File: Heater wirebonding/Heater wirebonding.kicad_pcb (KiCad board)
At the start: 2 copper layers, 22.8 x 19.5 mm, 2 parts, among them J1 Conn_01x20_Pin, J2 TF31-20S-0.5SH_800_

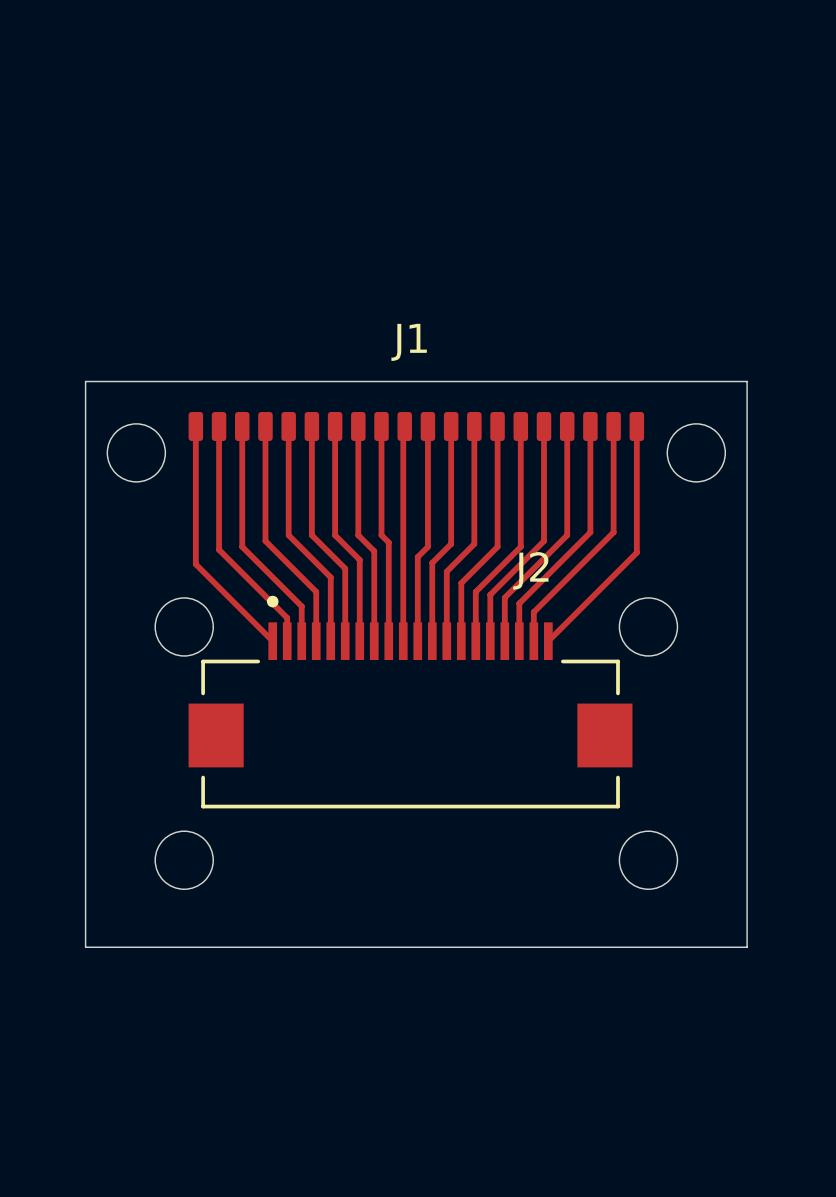
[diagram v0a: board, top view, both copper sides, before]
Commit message: Modified PCB layout to account for screw head
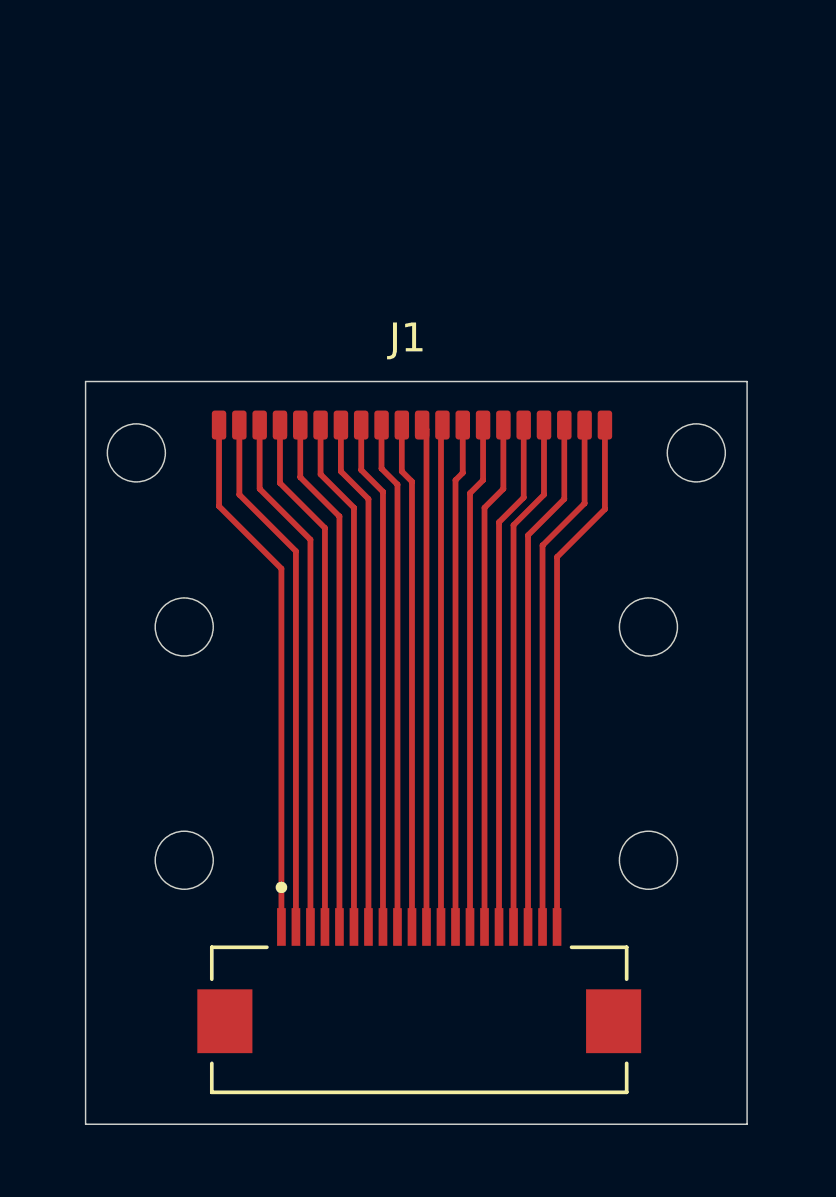
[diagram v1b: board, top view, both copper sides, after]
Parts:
- moved J2 9.85 mm to (160.0, 57.5)
- moved J1 0.16 mm to (159.6, 37.0)
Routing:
- net Net-(J1-Pin_9): track 7.50 -> 17.3 mm
- net Net-(J1-Pin_10): track 7.42 -> 17.2 mm
- net Net-(J1-Pin_8): track 7.63 -> 17.4 mm
- net Net-(J1-Pin_7): track 7.75 -> 17.5 mm
- net Net-(J1-Pin_6): track 7.88 -> 17.6 mm
- net Net-(J1-Pin_5): track 8.00 -> 17.7 mm
- net Net-(J1-Pin_4): track 8.12 -> 17.7 mm
- net Net-(J1-Pin_11): track 7.54 -> 17.2 mm
- net Net-(J1-Pin_3): track 8.25 -> 17.8 mm
- net Net-(J1-Pin_2): track 8.37 -> 17.9 mm
- net Net-(J1-Pin_1): track 8.50 -> 18.0 mm
- net Net-(J1-Pin_12): track 7.67 -> 17.1 mm
- net Net-(J1-Pin_13): track 7.79 -> 17.2 mm
- net Net-(J1-Pin_14): track 7.92 -> 17.3 mm
- net Net-(J1-Pin_15): track 8.04 -> 17.4 mm
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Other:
- board size 22.8 x 19.5 mm -> 22.8 x 25.6 mm

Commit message: Modified PCB design
Changed 4 wirebond pads to ground and filled in PCB GND zone. Changed PCB shape such that the PCB acts as the clamp for the chip.
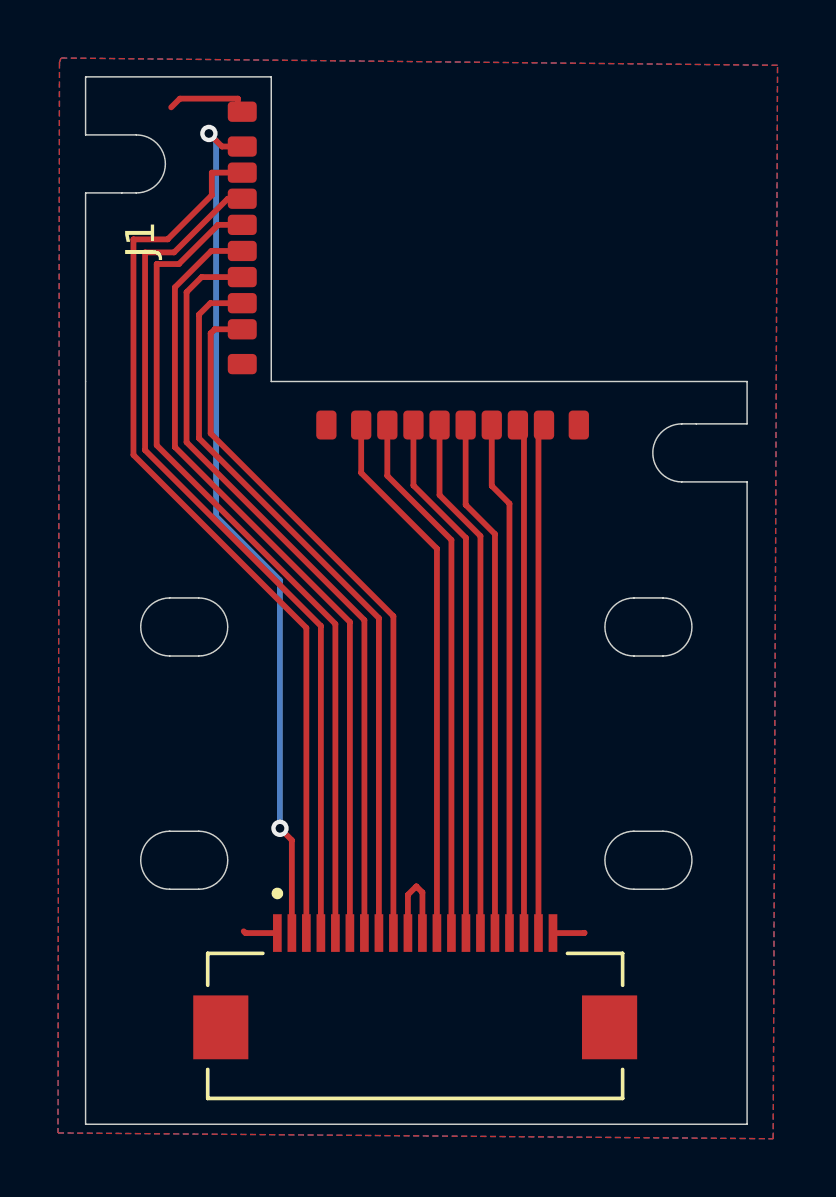
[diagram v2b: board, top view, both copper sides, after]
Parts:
- added J3: Conn_01x10_Pin, Custom_pads:Pads 1x10, F.Cu at (161.2, 37.0)
- J1: value Conn_01x20_Pin -> Conn_01x10_Pin; footprint Custom_pads:Pads 1x20 -> Custom_pads:Pads 1x10
- moved J1 8.57 mm to (153.9, 30.6), turned to 90 degrees
- moved J2 0.25 mm to (159.9, 57.7)
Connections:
- J1 pad 1: Net-(J1-Pin_1) -> GND
- J1 pad 10: Net-(J1-Pin_10) -> GND
- J2 pad 1: Net-(J1-Pin_1) -> GND
- J2 pad 10: Net-(J1-Pin_10) -> GND
- J2 pad 11: Net-(J1-Pin_11) -> GND
- J2 pad 12: Net-(J1-Pin_12) -> Net-(J3-Pin_9)
- J2 pad 13: Net-(J1-Pin_13) -> Net-(J3-Pin_8)
- J2 pad 14: Net-(J1-Pin_14) -> Net-(J3-Pin_7)
- J2 pad 15: Net-(J1-Pin_15) -> Net-(J3-Pin_6)
- J2 pad 16: Net-(J1-Pin_16) -> Net-(J3-Pin_5)
- J2 pad 17: Net-(J1-Pin_17) -> Net-(J3-Pin_4)
- J2 pad 18: Net-(J1-Pin_18) -> Net-(J3-Pin_3)
- J2 pad 19: Net-(J1-Pin_19) -> Net-(J3-Pin_2)
- J2 pad 2: Net-(J1-Pin_2) -> Net-(J1-Pin_9)
- J2 pad 20: Net-(J1-Pin_20) -> GND
- J2 pad 3: Net-(J1-Pin_3) -> Net-(J1-Pin_8)
- J2 pad 4: Net-(J1-Pin_4) -> Net-(J1-Pin_7)
- J2 pad 5: Net-(J1-Pin_5) -> Net-(J1-Pin_6)
- J2 pad 6: Net-(J1-Pin_6) -> Net-(J1-Pin_5)
- J2 pad 7: Net-(J1-Pin_7) -> Net-(J1-Pin_4)
- J2 pad 8: Net-(J1-Pin_8) -> Net-(J1-Pin_3)
- J2 pad 9: Net-(J1-Pin_9) -> Net-(J1-Pin_2)
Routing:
- net Net-(J3-Pin_9): track 0.00 -> 18.6 mm
- net Net-(J3-Pin_8): track 0.00 -> 18.4 mm
- net Net-(J3-Pin_7): track 0.00 -> 18.3 mm
- net Net-(J3-Pin_6): track 0.00 -> 18.1 mm
- net Net-(J1-Pin_1): track 18.0 -> 0.00 mm
- net Net-(J3-Pin_5): track 0.00 -> 17.9 mm
- net Net-(J1-Pin_20): track 17.8 -> 0.00 mm
- net Net-(J3-Pin_4): track 0.00 -> 17.8 mm
- net Net-(J1-Pin_19): track 17.7 -> 0.00 mm
- net Net-(J1-Pin_18): track 17.6 -> 0.00 mm
- net Net-(J3-Pin_3): track 0.00 -> 17.6 mm
- net Net-(J3-Pin_2): track 0.00 -> 17.6 mm
- net Net-(J1-Pin_17): track 17.5 -> 0.00 mm
- net Net-(J1-Pin_16): track 17.5 -> 0.00 mm
- net Net-(J1-Pin_15): track 17.4 -> 0.00 mm
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- added copper zone on B.Cu, net GND
- added copper zone on F.Cu, net GND
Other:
- board size 22.8 x 25.6 mm -> 22.8 x 36.1 mm
